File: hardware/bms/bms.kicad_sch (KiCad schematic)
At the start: 33 parts

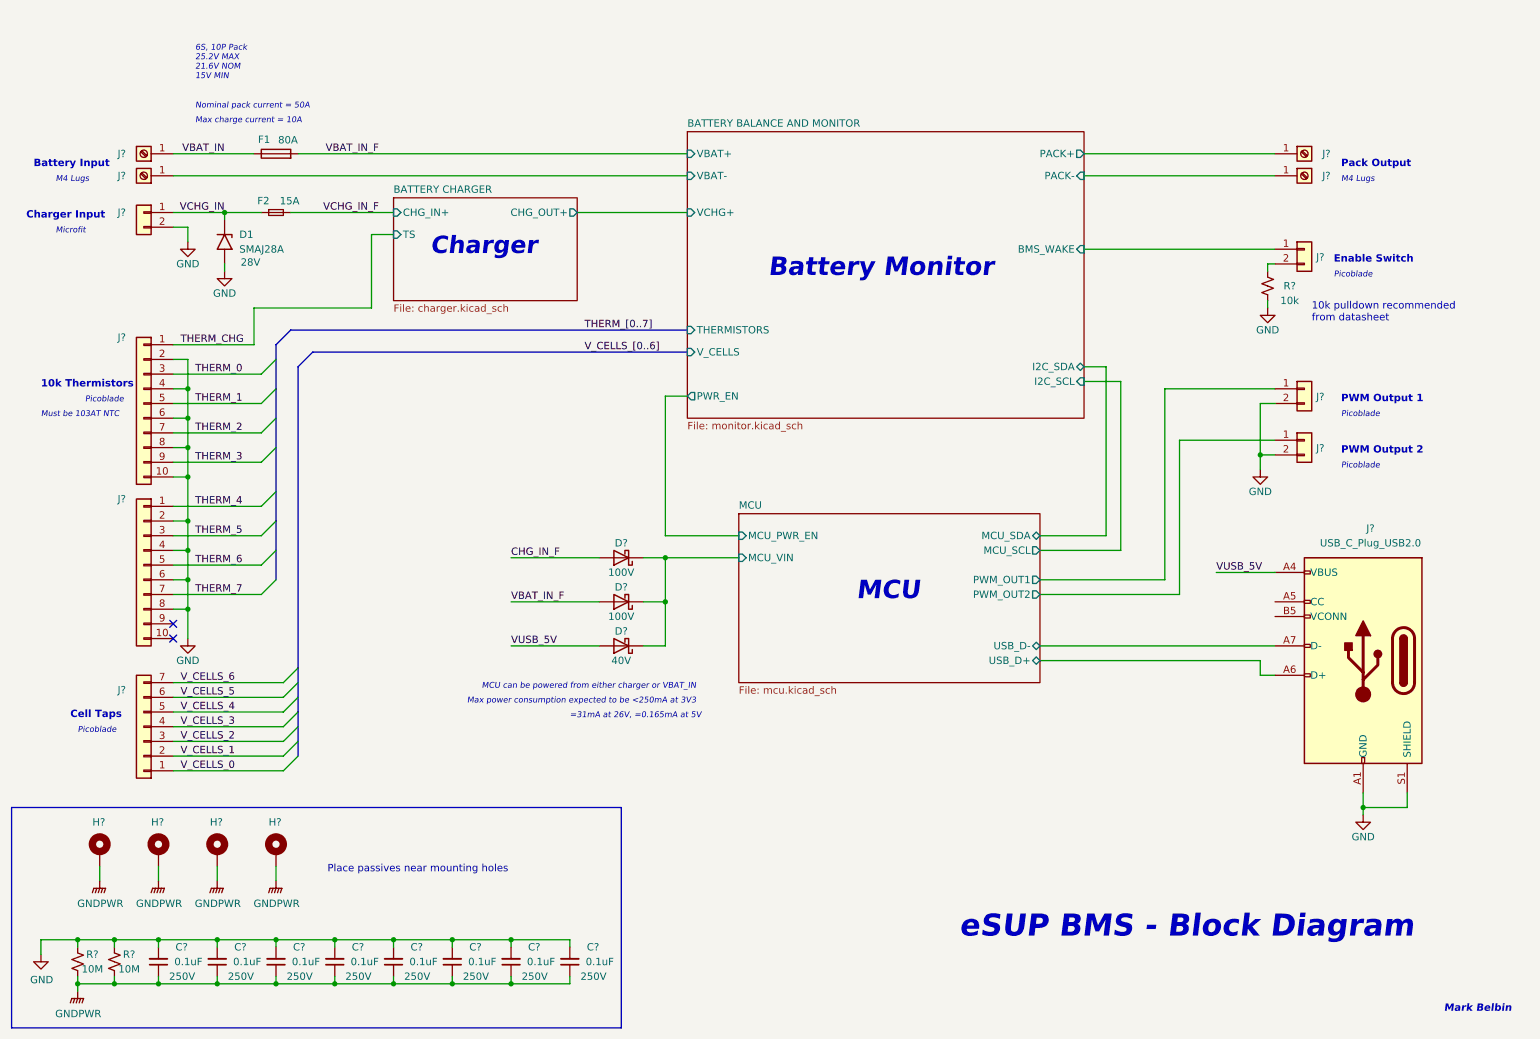
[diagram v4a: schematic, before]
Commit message: Charger schematic complete! Only MCU left.
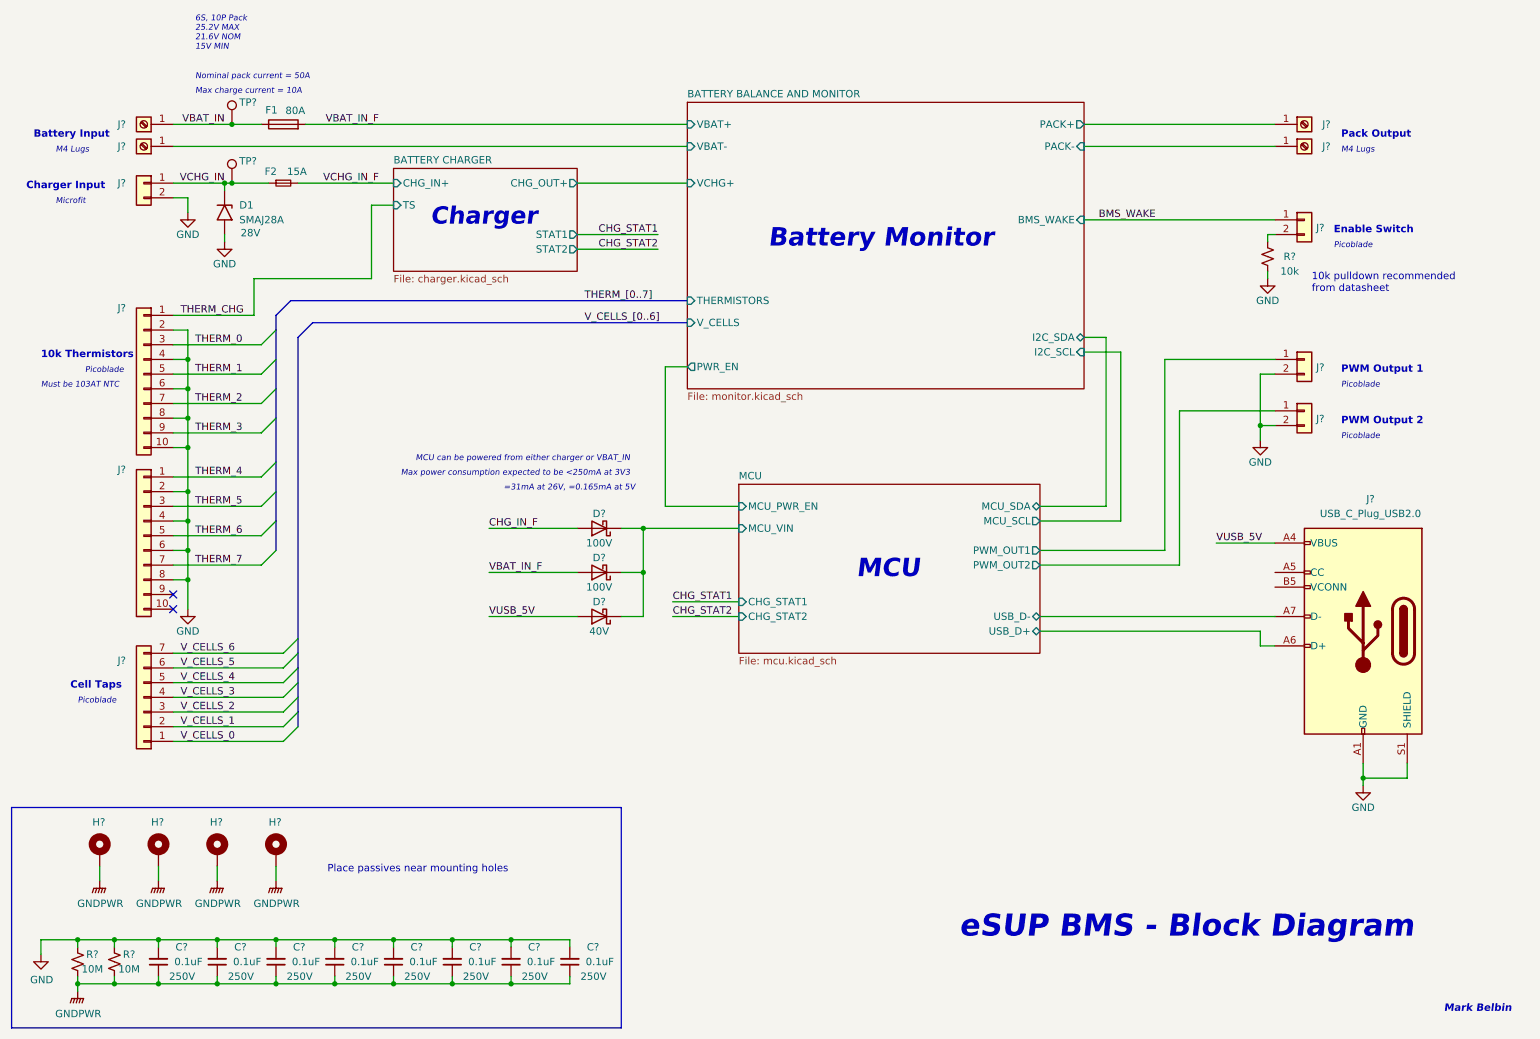
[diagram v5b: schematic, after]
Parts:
- added TP? (x2): TestPoint, TestPoint:TestPoint_Pad_D1.0mm, symbol Connector:TestPoint
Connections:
- net VBAT_IN: now also TP?.1
- net VCHG_IN: now also TP?.1
- net BATTERY BALANCE AND MONITOR/BMS_WAKE renamed BMS_WAKE
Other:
- sheet BATTERY CHARGER ports: added STAT1, STAT2; removed none
- sheet MCU ports: added CHG_STAT1, CHG_STAT2; removed none
- moved on the sheet: D1, D?, F1, F2, J?, R?

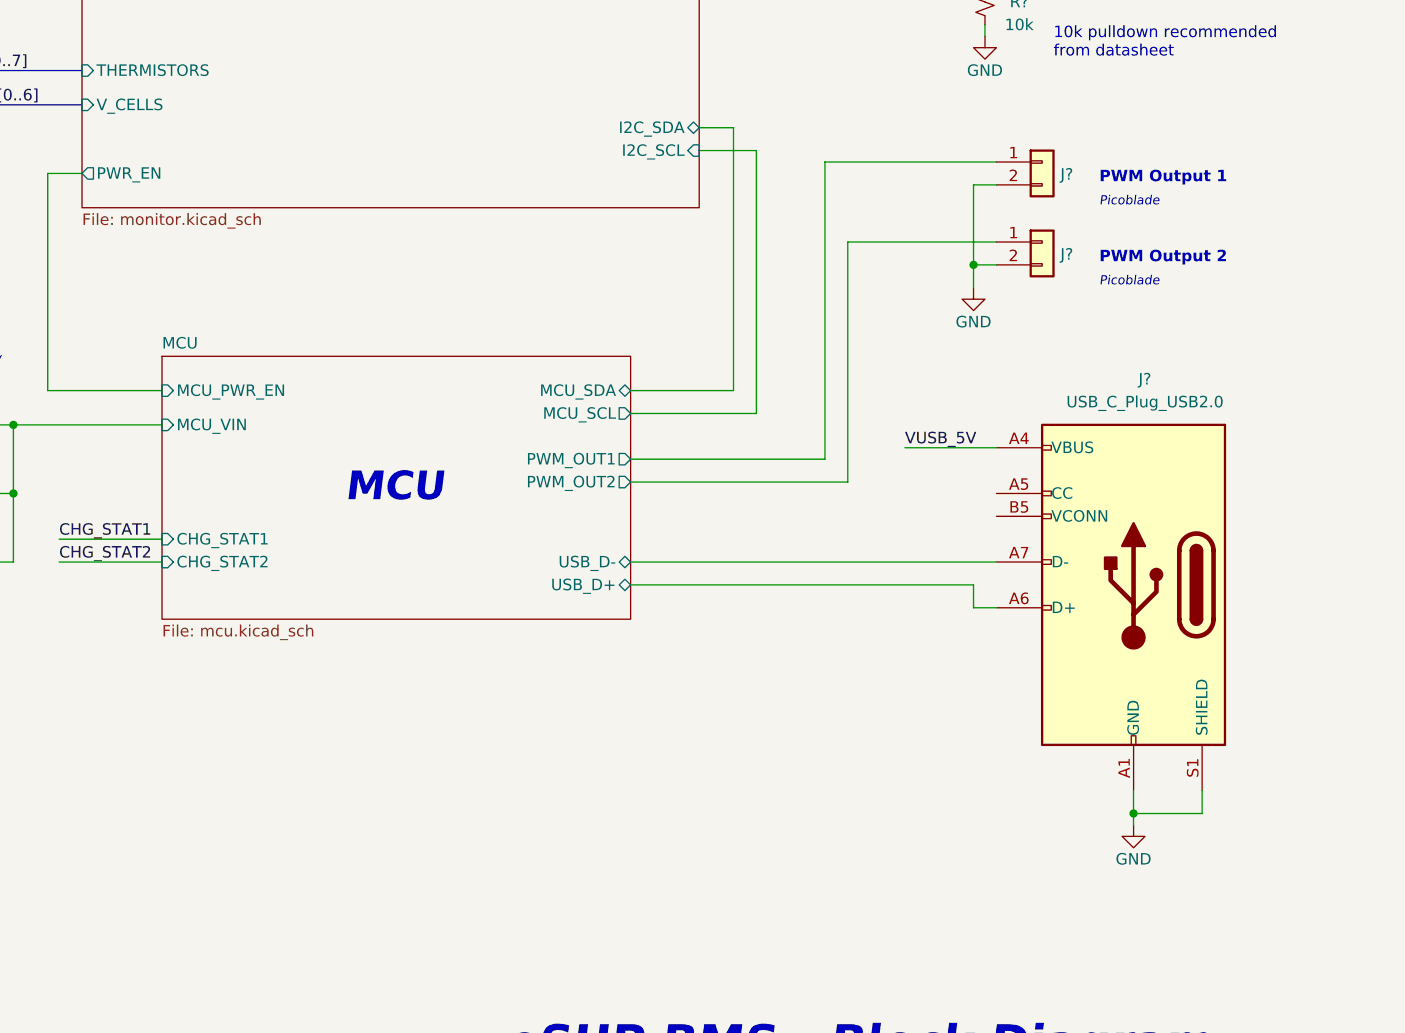
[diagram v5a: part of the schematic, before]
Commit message: Choose MCU as ESP32-C3-MINI. Small form factor with just enough I/O.
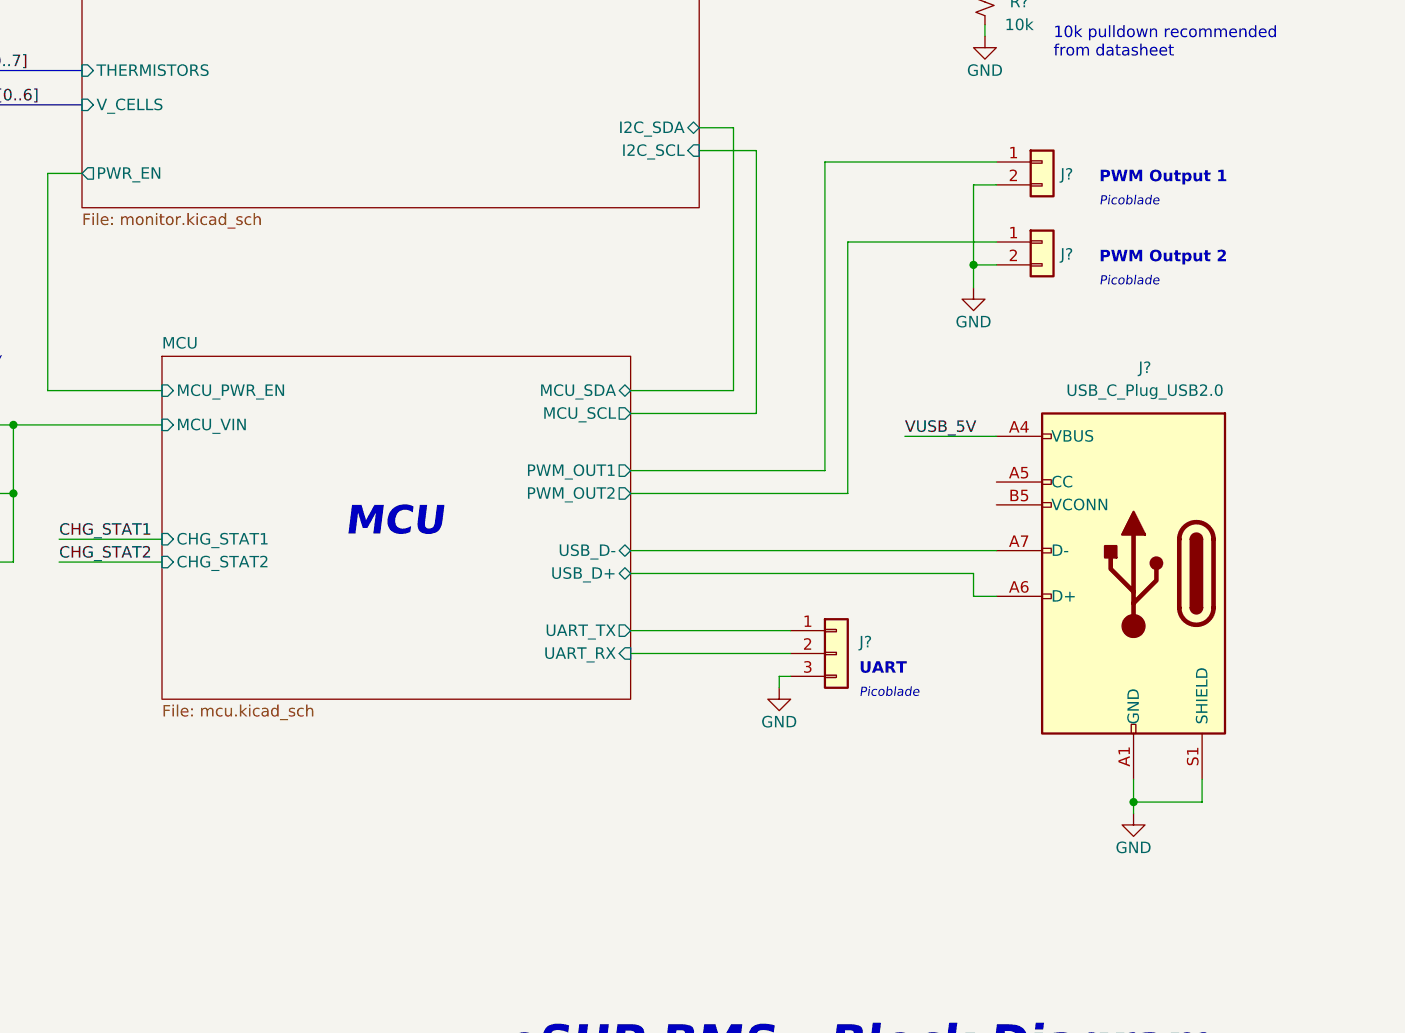
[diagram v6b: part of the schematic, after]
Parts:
- added J?: Conn_01x03, Connector_Molex:Molex_PicoBlade_53261-0371_1x03-1MP_P1.25mm_Horizontal, symbol Connector_Generic:Conn_01x03
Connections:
- net GND: now also J?.3 (Pin_3)
- new net MCU/UART_RX: J?.2 (Pin_2)
- new net MCU/UART_TX: J?.1 (Pin_1)
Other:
- sheet MCU ports: added UART_RX, UART_TX; removed none
- note added: "UART"
- moved on the sheet: J?

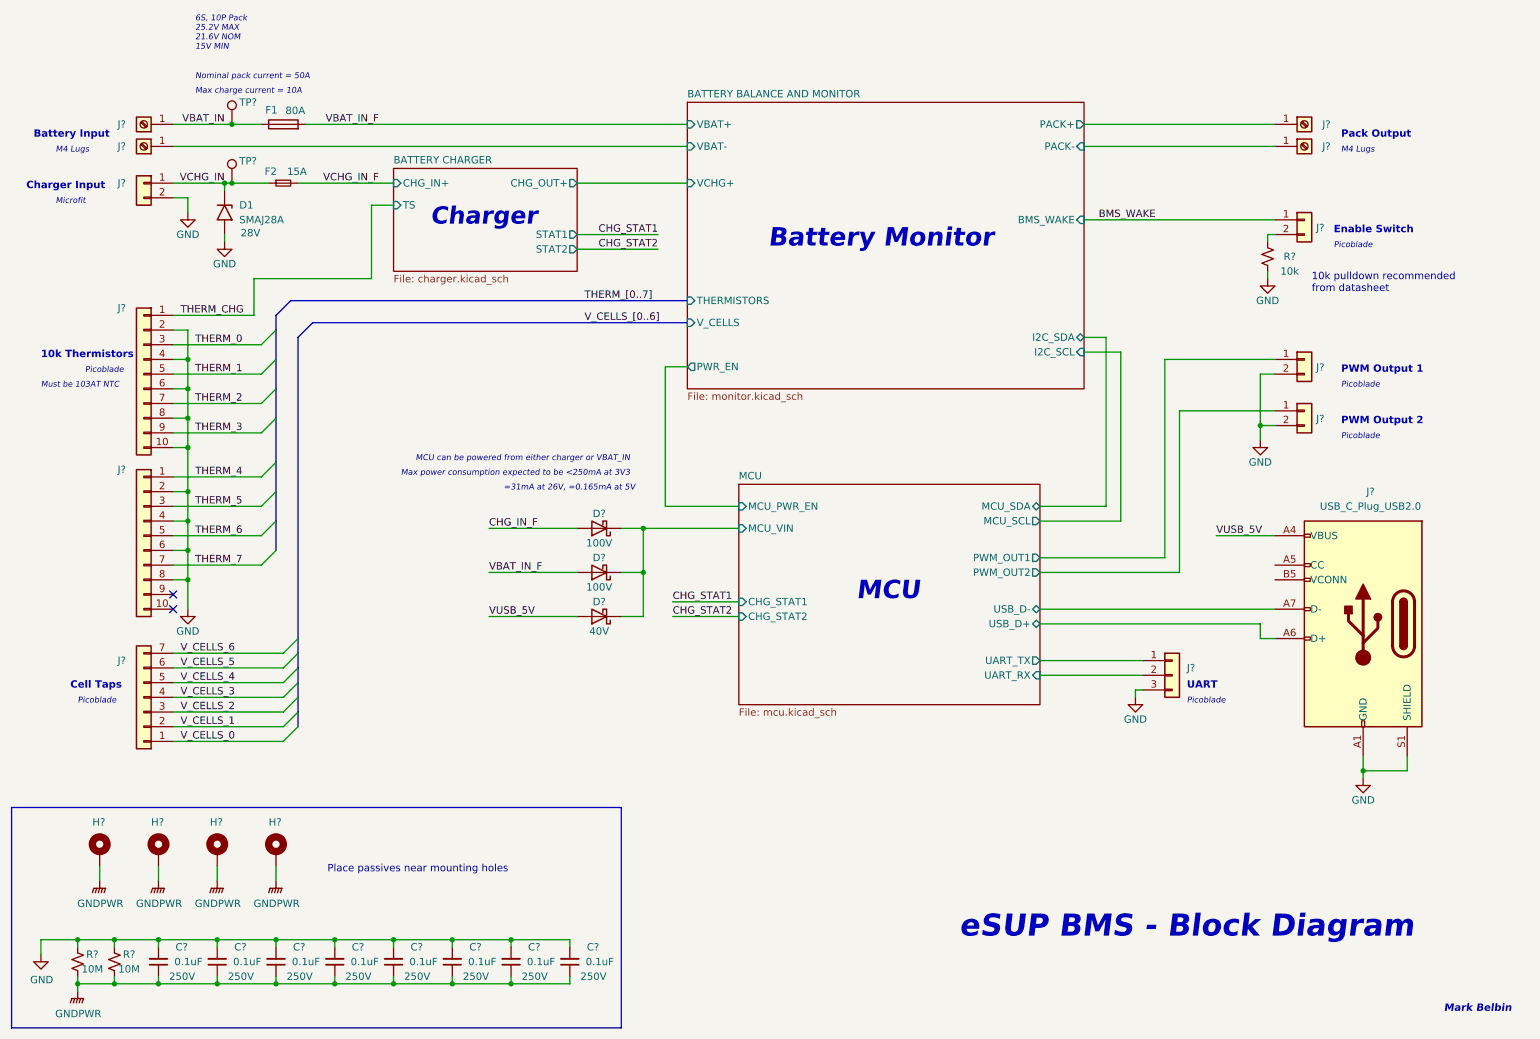
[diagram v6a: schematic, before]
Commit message: Added BJT to enable BMS/MCU when charger input voltage present
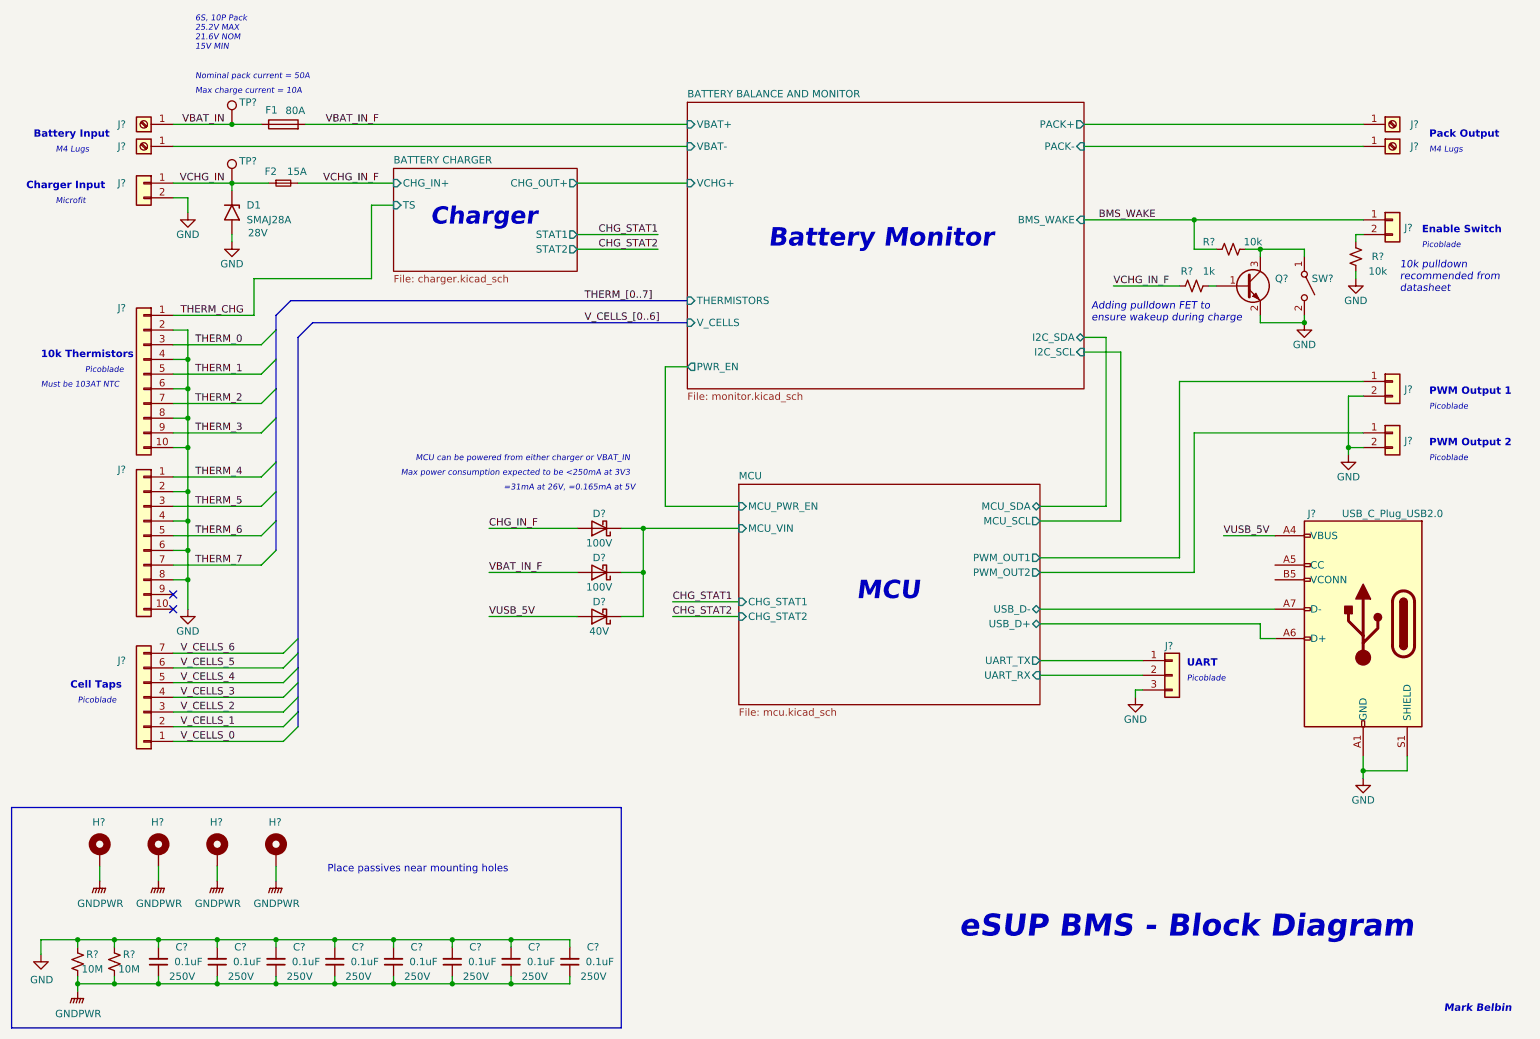
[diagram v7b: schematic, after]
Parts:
- added Q?: MMBT3904, Package_TO_SOT_SMD:SOT-23, symbol Transistor_BJT:MMBT3904
- added R?: 1k, Resistor_SMD:R_0603_1608Metric, symbol Device:R_Small_US
- added R?: 10k, Resistor_SMD:R_0603_1608Metric, symbol Device:R_Small_US
- added SW?: SW_SPST, bms:SW_DS04-254-2-01BK-SMT-TR, symbol Switch:SW_SPST
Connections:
- net BMS_WAKE: now also R?.1
- net GND: now also Q?.2 (E), SW?.2 (B)
- net VCHG_IN_F: now also R?.2
- new net: Q?.1 (B), R?.1
- new net: Q?.3 (C), R?.2, SW?.1 (A)
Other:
- note added: "Adding pulldown FET to ensure wakeup during charge"
- moved on the sheet: D1, J?, R?
